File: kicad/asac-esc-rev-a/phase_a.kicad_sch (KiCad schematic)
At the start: 18 parts

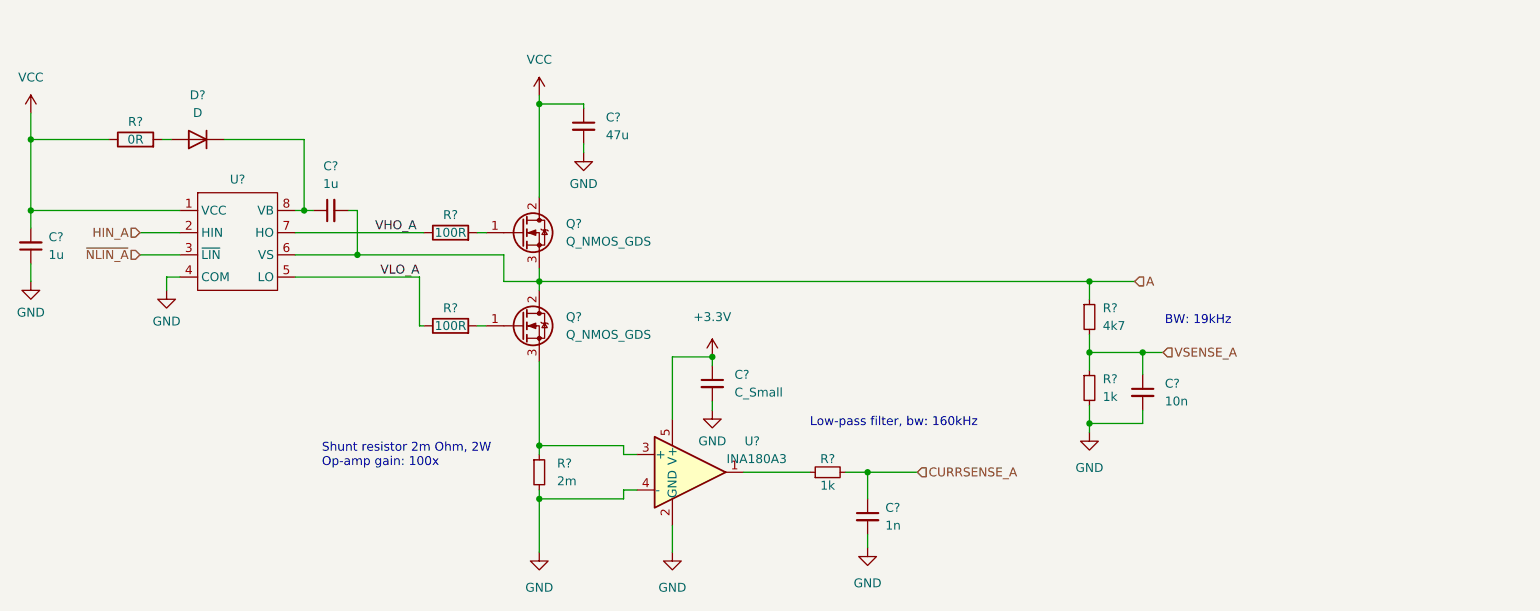
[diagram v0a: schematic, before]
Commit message: Changed from current sensing each phase to a single current sensing circuit for all MOSFETs. Primary motivation is that it's simpler, let's just hope that it works OK...!
Pretty much done with schematic now, everything is not
connected to the MCU yet however, since the layout might
have an impact on exactly which port should be connected
where.
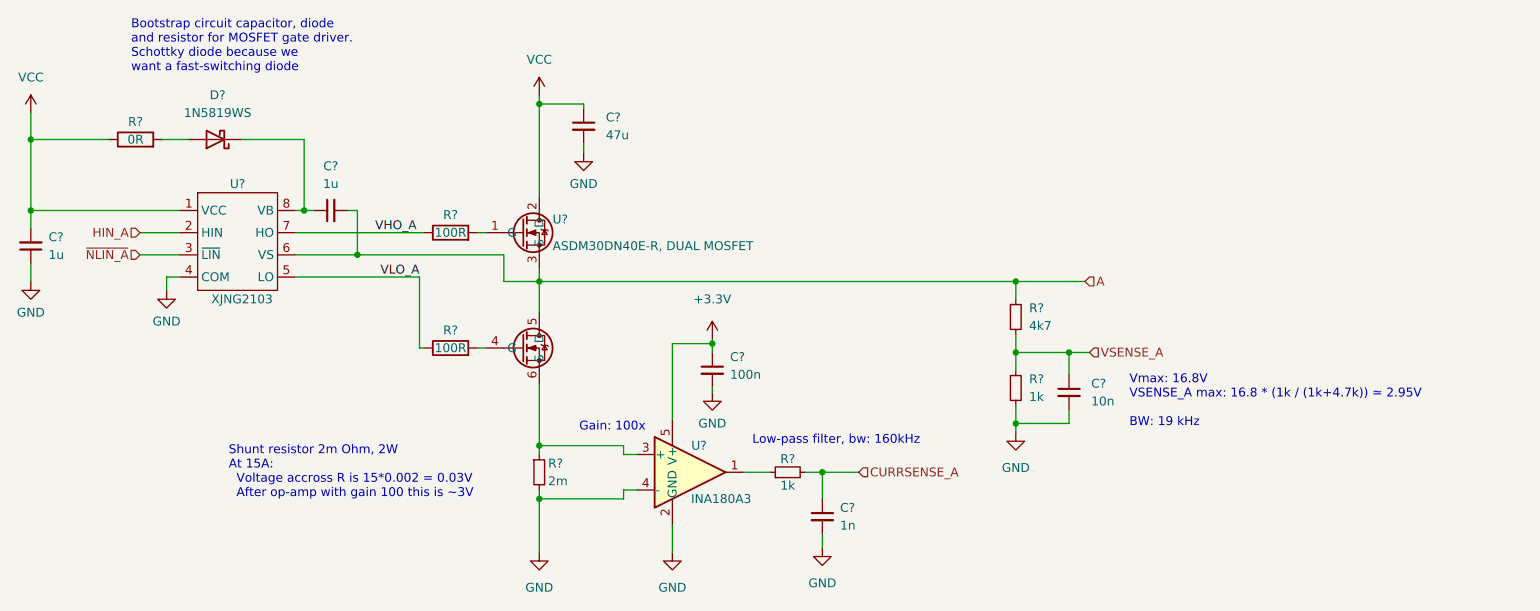
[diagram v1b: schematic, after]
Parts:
- removed D?: D, symbol Device:D
- removed Q? (x2): Q_NMOS_GDS, symbol Device:Q_NMOS_GDS
- added D?: 1N5819WS, Diode_SMD:D_SOD-323, symbol Diode:1N5819WS
- added U?: ASDM30DN40E-R, DUAL MOSFET, Custom:PDFN3333-8_L3.2-W3.1-P0.65-LS3.4-BL, symbol Custom2:ASDM30DN40E-R_MOSFET_DUAL
- C? (x4): footprint (none) -> Capacitor_SMD:C_0402_1005Metric
- C?: value C_Small -> 100n; footprint (none) -> Capacitor_SMD:C_0402_1005Metric
- C?: footprint (none) -> Capacitor_SMD:C_1206_3216Metric
- R? (x4): footprint (none) -> Resistor_SMD:R_0402_1005Metric
- R? (x2): footprint (none) -> Resistor_SMD:R_0603_1608Metric
- R?: footprint (none) -> Resistor_SMD:R_2512_6332Metric; Name (none) -> FMF25JPJR002XLH
- U?: value XJNG2103_MOSFET_GATE_DRIVER -> XJNG2103; Name (none) -> XJNG2103
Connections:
- net A: now also U?.3 (S), U?.5 (D)
- net VCC: now also U?.2 (D)
- net at R?.2: now also U?.4 (G)
- net at R?.1, U?.3 (+): now also U?.6 (S)
- net at C?.1, U?.8 (VB): now also D?.1 (K)
- net at R?.2: now also U?.1 (G)
- net at R?.2: now also D?.2 (A)
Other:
- note added: "Bootstrap circuit capacitor, diode and resistor for MOSFET gate driver. Schottky diode because we want a fast-switching diode"
- note added: "Gain: 100x"
- note added: "Shunt resistor 2m Ohm, 2W At 15A: Voltage accross R is 15*0.002 = 0.03V After op-amp with gain 100 this is ~3V"
- note added: "Vmax: 16.8V VSENSE_A max: 16.8 * (1k / (1k+4.7k)) ≃ 2.95V BW: 19 kHz"
- note removed: "BW: 19kHz"
- note removed: "Shunt resistor 2m Ohm, 2W Op-amp gain: 100x"
- moved on the sheet: C?, R?
